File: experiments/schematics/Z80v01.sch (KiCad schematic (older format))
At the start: 62 parts

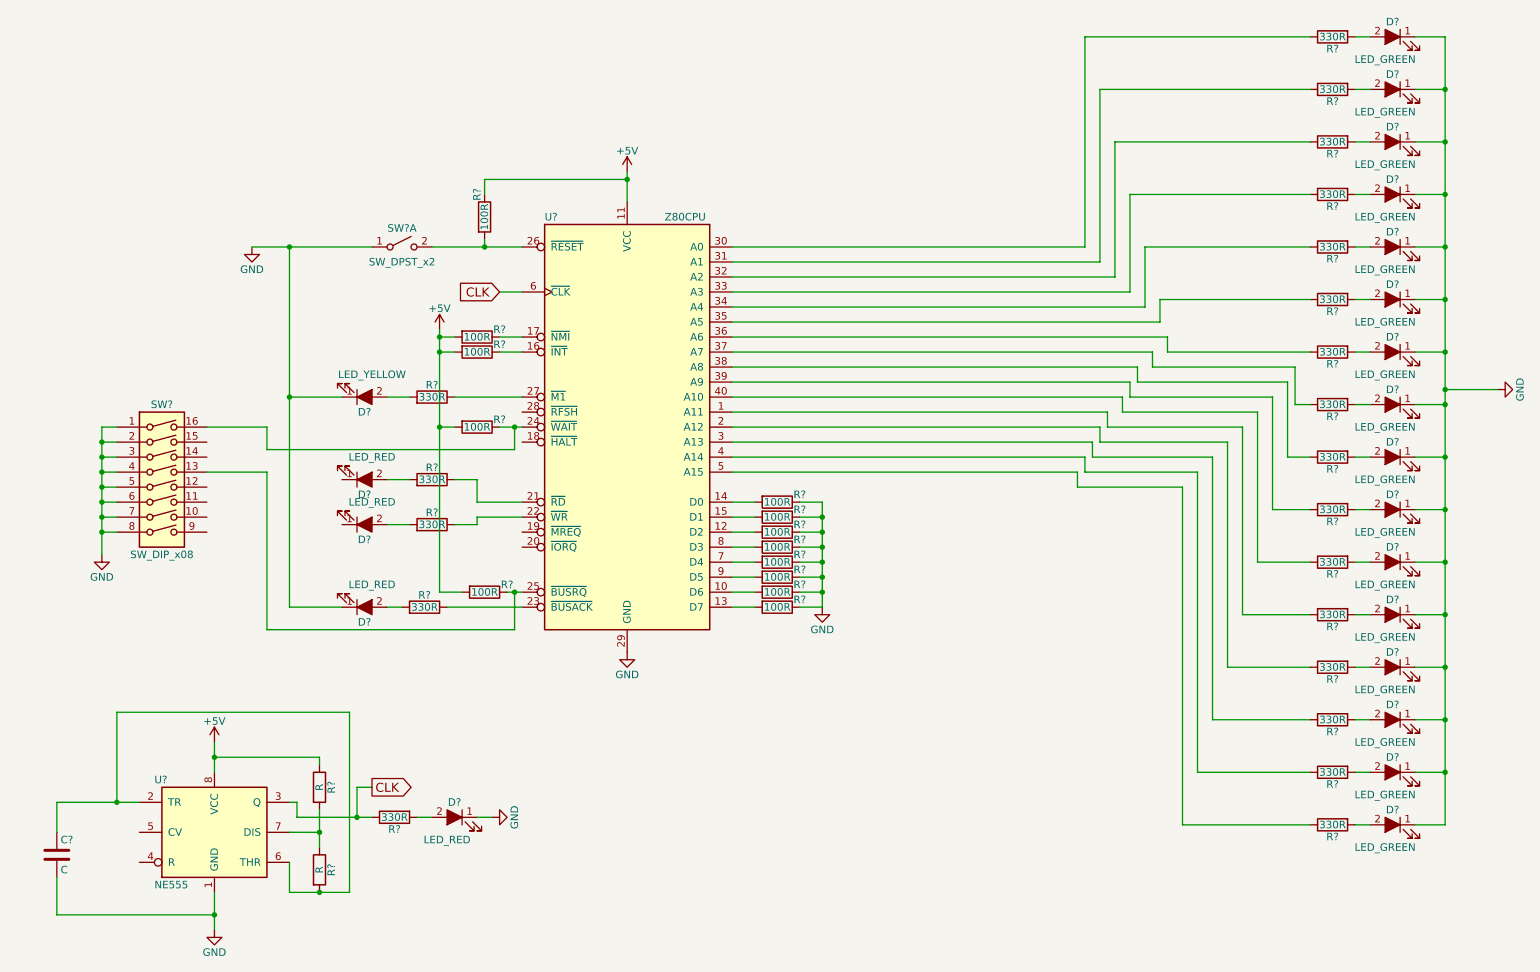
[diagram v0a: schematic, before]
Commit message: Using sheets to separate experiments
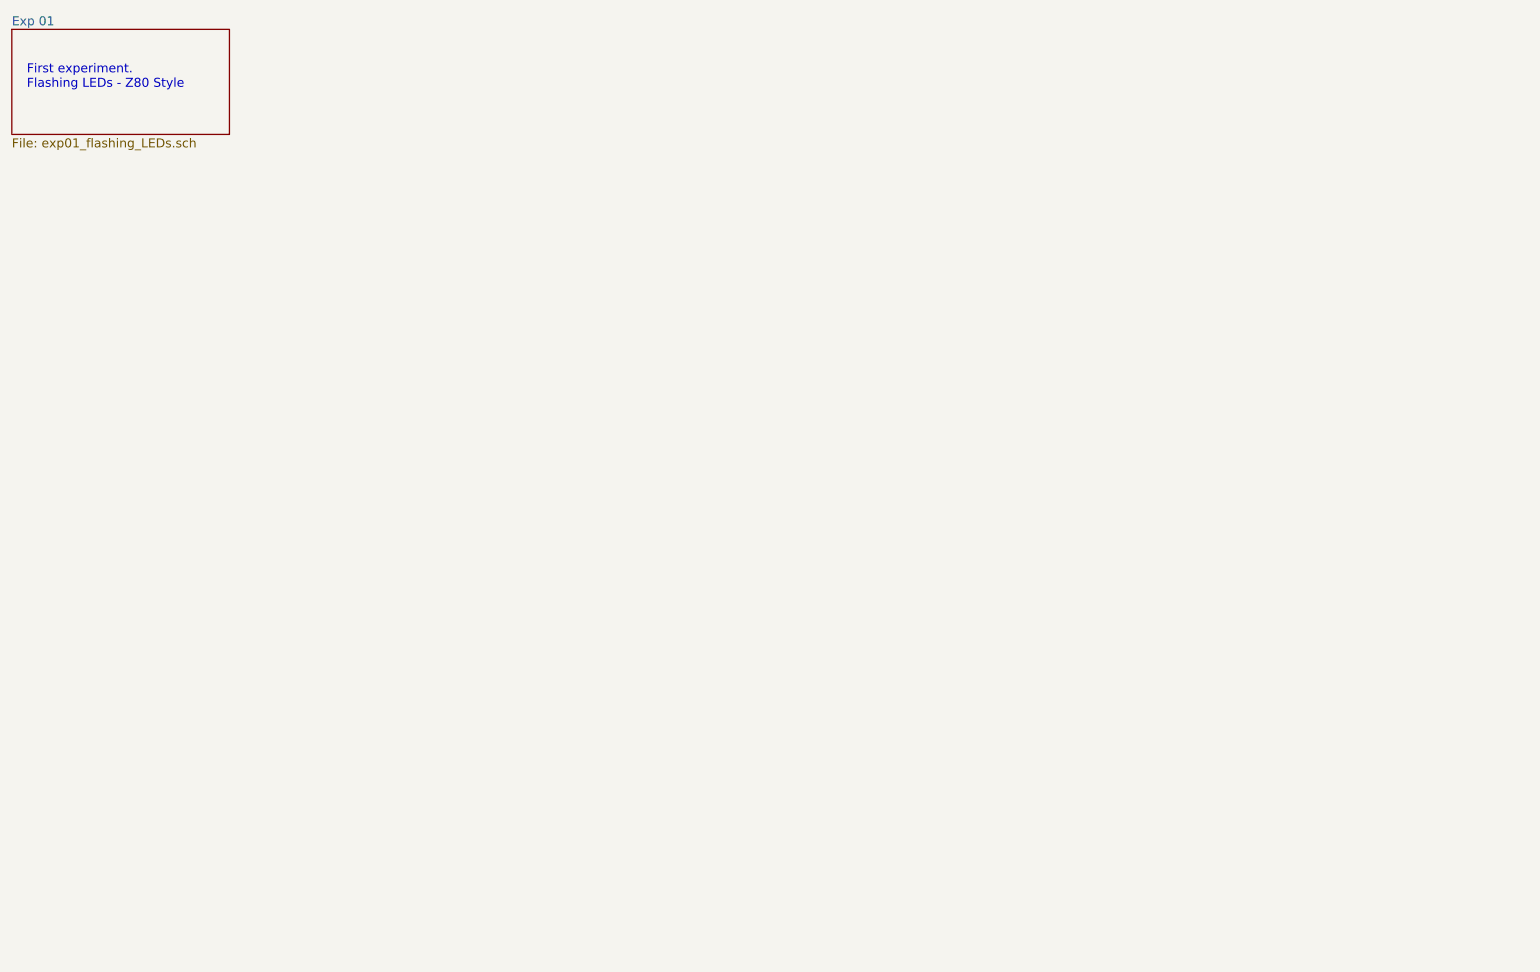
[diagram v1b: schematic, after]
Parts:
- removed C?: C, symbol C
- removed D? (x16): LED_GREEN, symbol LED_ALT
- removed D?: LED_YELLOW, symbol LED_ALT
- removed D? (x4): LED_RED, symbol LED_ALT
- removed R? (x21): 330R, symbol R
- removed R? (x13): 100R, symbol R
- removed R? (x2): R, symbol R
- removed SW?: SW_DPST_x2, symbol SW_DPST_x2
- removed SW?: SW_DIP_x08, symbol SW_DIP_x08
- removed U?: Z80CPU, symbol Z80CPU
- removed U?: NE555, symbol NE555
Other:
- note added: "First experiment.\nFlashing LEDs - Z80 Style"
